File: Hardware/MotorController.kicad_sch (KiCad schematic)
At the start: 9 parts, among them U4 STSPIN250

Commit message: BIG Changes
Create a 4 Layer Variation
Change Motor Controller routing.
Change Power Regulation.
Optimize Sensor routing.
Pray I know what i'm doing
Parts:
- removed C3: 22 uF, Capacitor_SMD:C_0805_2012Metric, symbol Device:C_Polarized_Small
- C4, Coff1: footprint Capacitor_SMD:C_0805_2012Metric -> Capacitor_SMD:C_0603_1608Metric
- Cr1: value 10000 pF -> 10 nF; footprint Capacitor_SMD:C_0805_2012Metric -> Capacitor_SMD:C_0603_1608Metric
- Roff1, Roff2, Rr1: footprint Resistor_SMD:R_0805_2012Metric -> Resistor_SMD:R_0603_1608Metric
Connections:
- net +3V3 renamed V_BAT
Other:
- moved on the sheet: C4

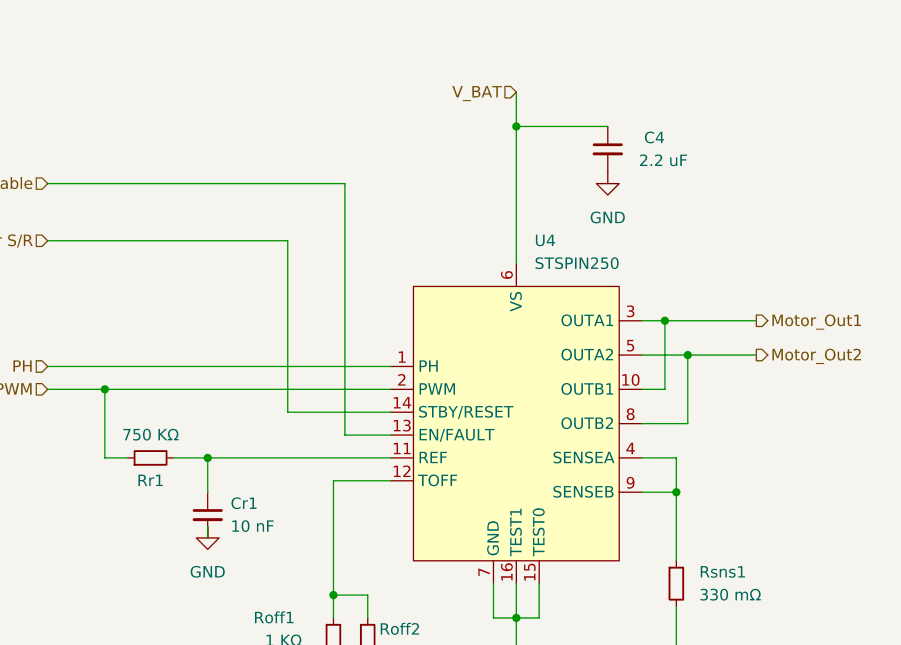
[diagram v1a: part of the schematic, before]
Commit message: 4 L:ayer Board with USB-C
Created a 4-Layer PCB with USB-C updates
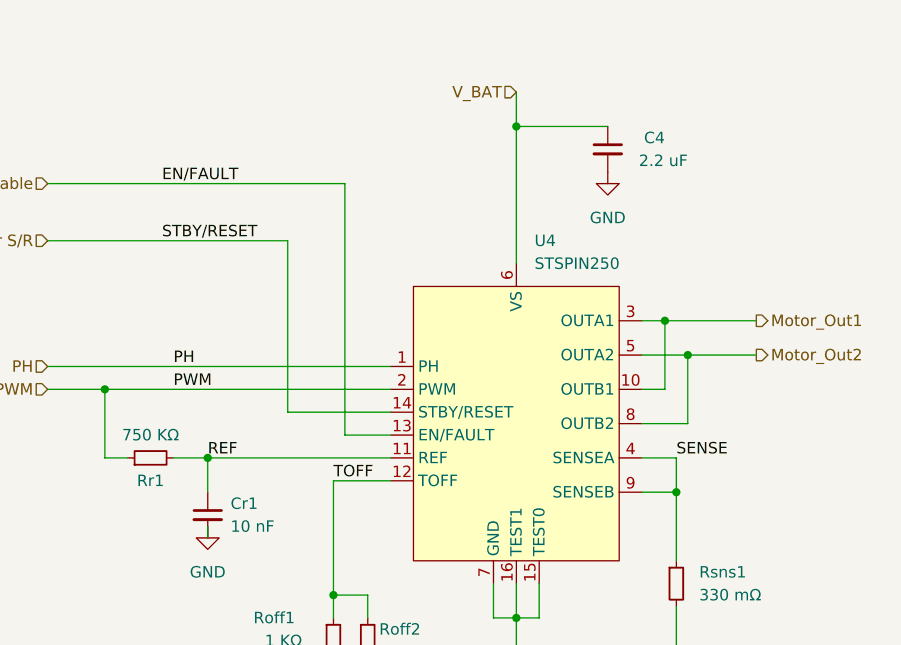
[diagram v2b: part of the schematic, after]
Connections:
- net SENSE: now reaches Rsns1.1, U4.4 (SENSEA), U4.9 (SENSEB)
- net TOFF: now reaches Roff1.1, Roff2.1, U4.12 (TOFF)
- net REF: now reaches Cr1.1, Rr1.2, U4.11 (REF)
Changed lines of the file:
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@@
+    (effects (font (size 1.27 1.27)) (justify left bottom))
+  )
+  (label "EN{slash}FAULT" (at 109.22 86.36 0) (fields_autoplaced)
+    (effects (font (size 1.27 1.27)) (justify left bottom))
+  )
+  (label "TOFF" (at 128.27 119.38 0) (fields_autoplaced)
+    (effects (font (size 1.27 1.27)) (justify left bottom))
+  )
+  (label "REF" (at 114.3 116.84 0) (fields_autoplaced)
+    (effects (font (size 1.27 1.27)) (justify left bottom))
+  )
+  (label "PWM" (at 110.49 109.22 0) (fields_autoplaced)
+    (effects (font (size 1.27 1.27)) (justify left bottom))
+  )
+  (label "PH" (at 110.49 106.68 0) (fields_autoplaced)
+    (effects (font (size 1.27 1.27)) (justify left bottom))
+  )
+  (label "STBY{slash}RESET" (at 109.22 92.71 0) (fields_autoplaced)
+    (effects (font (size 1.27 1.27)) (justify left bottom))
+  )
+  (label "SENSE" (at 166.37 116.84 0) (fields_autoplaced)
     (effects (font (size 1.27 1.27)) (justify left bottom))
   )
